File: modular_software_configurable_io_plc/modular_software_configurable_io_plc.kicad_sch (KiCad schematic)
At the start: 8 parts, among them J1 FW-14-03-G-D-085-315, J2 FW-02-03-G-D-085-315, J3 FW-02-03-G-D-085-315, J4 FW-04-03-G-D-085-315, J5 FW-04-03-G-D-085-315, J6 FW-02-03-G-D-085-315, J7 FW-02-03-G-D-085-315, J8 FW-14-03-G-D-085-315

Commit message: Minor updates to project files
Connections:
- net GNDA: now also J1.1, J1.11, J1.13, J1.15, J1.17, J1.19, J1.21, J1.23, J1.25, J1.27, J1.3, J1.5, J1.7, J1.9, J8.10, J8.12, J8.14, J8.16, J8.18, J8.2, J8.20, J8.22, J8.24, J8.26, J8.28, J8.4, J8.6, J8.8

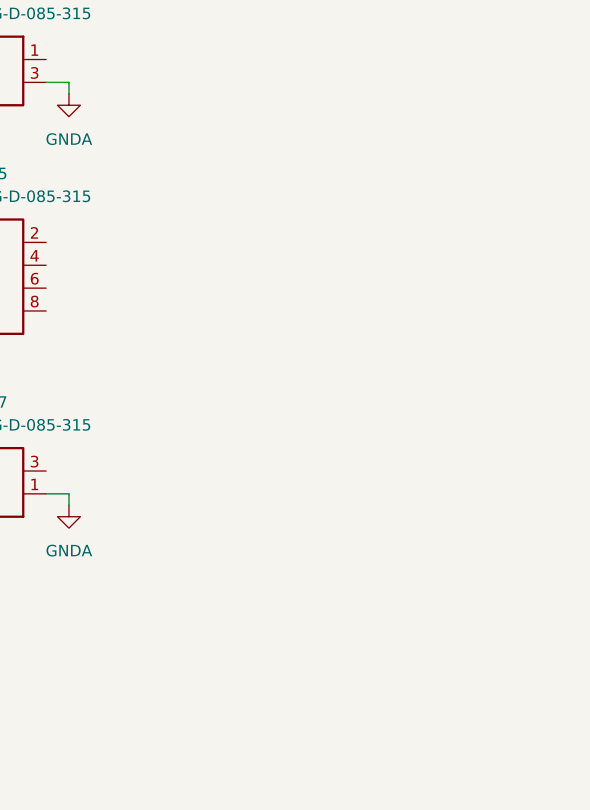
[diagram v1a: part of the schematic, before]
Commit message: Update KiCAD Symbol Generator submodule and add ibom configuration file
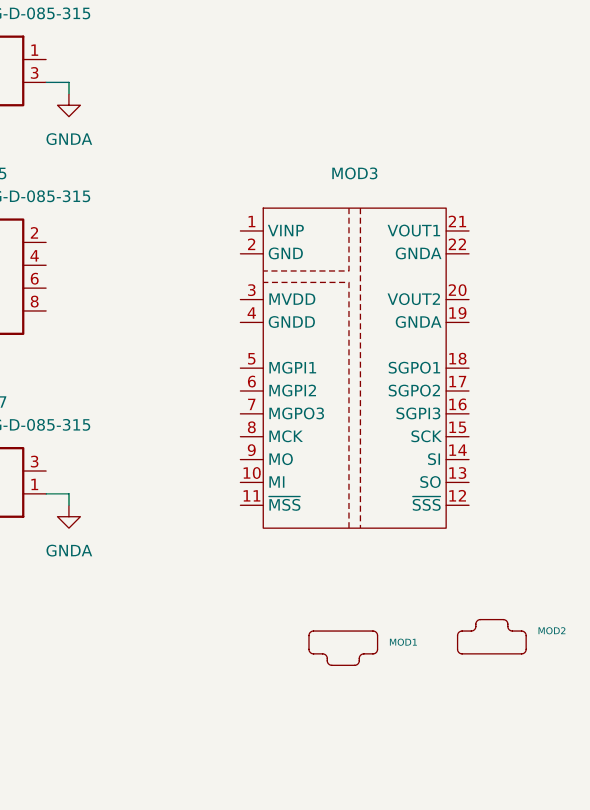
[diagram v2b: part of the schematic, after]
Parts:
- added MOD1: ~, modules_footprints:minimal_ad74413r, symbol UNITED_MODULES_DATA_BASE:MINIMAL_AD74413R
- added MOD2: ~, modules_footprints:minimal_max14906, symbol UNITED_MODULES_DATA_BASE:MINIMAL_MAX14906
- added MOD3: ~, modules_footprints:minimal_adp1032, symbol UNITED_MODULES_DATA_BASE:MINIMAL_ADP1032
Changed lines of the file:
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@@
+	)
+	(symbol
+		(lib_id "UNITED_MODULES_DATA_BASE:MINIMAL_ADP1032")
+		(at 217.17 100.33 0)
+		(unit 1)
+		(exclude_from_sim no)
+		(in_bom yes)
+		(on_board yes)
+		(dnp no)
+		(fields_autoplaced yes)
+		(property "Reference" "MOD3"
+			(at 217.17 78.74 0)
+			(effects
+				(font
+					(size 1.27 1.27)
+				)
+			)
+		)
+		(property "Value" "~"
+			(at 217.17 81.28 0)
+			(effects
+				(font
+					(size 1.27 1.27)
+				)
+			)
+		)
+		(property "Footprint" "modules_footprints:minimal_adp1032"
+			(at 227.33 120.65 0)
+			(effects
+				(font
+					(size 1.27 1.27)
+				)
+				(justify left)
+				(hide yes)
+			)
+		)
+		(property "Datasheet" ""
+			(at 217.17 95.25 0)
+			(effects
+				(font
+					(size 1.27 1.27)
+				)
+				(hide yes)
+			)
+		)
+		(property "Description" ""
+			(at 217.17 95.25 0)
+			(effects
+				(font
+					(size 1.27 1.27)
+				)
+				(hide yes)
+			)
+		)
+		(pin "13"
+		)
+		(pin "10"
+		)
+		(pin "19"
+		)
+		(pin "2"
+		)
+		(pin "17"
+		)
+		(pin "20"
+		)
+		(pin "15"
+		)
+		(pin "22"
+		)
+		(pin "7"
+		)
+		(pin "16"
+		)
+		(pin "8"
+		)
+		(pin "12"
+		)
+		(pin "4"
+		)
+		(pin "5"
+		)
+		(pin "3"
+		)
+		(pin "18"
+		)
+		(pin "6"
+		)
+		(pin "11"
+		)
+		(pin "14"
+		)
+		(pin "21"
+		)
+		(pin "1"
+		)
+		(pin "9"
+		)
+		(instances
+			(project ""
+				(path "/b764ffe3-5231-4422-b46d-b0de4c44c7b4"
+					(reference "MOD3")
+					(unit 1)
+				)
+			)
+		)
 	)
 	(symbol
@@
 	)
 	(symbol
+		(lib_id "UNITED_MODULES_DATA_BASE:MINIMAL_AD74413R")
+		(at 215.9 130.81 0)
+		(unit 1)
+		(exclude_from_sim no)
+		(in_bom yes)
+		(on_board yes)
+		(dnp no)
+		(fields_autoplaced yes)
+		(property "Reference" "MOD1"
+			(at 220.98 130.81 0)
+			(effects
+				(font
+					(size 0.762 0.762)
+				)
+				(justify left)
+			)
+		)
+		(property "Value" "~"
+			(at 220.98 132.08 0)
+			(effects
+				(font
+					(size 1.27 1.27)
+				)
+				(justify left)
+			)
+		)
+		(property "Footprint" "modules_footprints:minimal_ad74413r"
+			(at 218.44 135.89 0)
+			(effects
+				(font
+					(size 1.27 1.27)
+				)
+				(justify left)
+				(hide yes)
+			)
+		)
+		(property "Datasheet" ""
+			(at 215.9 130.81 0)
+			(effects
+				(font
+					(size 1.27 1.27)
+				)
+				(hide yes)
+			)
+		)
+		(property "Description" ""
+			(at 215.9 130.81 0)
+			(effects
+				(font
+					(size 1.27 1.27)
+				)
+				(hide yes)
+			)
+		)
+		(instances
+			(project ""
+				(path "/b764ffe3-5231-4422-b46d-b0de4c44c7b4"
+					(reference "MOD1")
+					(unit 1)
+				)
+			)
+		)
+	)
+	(symbol
 		(lib_id "power:GNDA")
 		(at 185.42 69.85 0)
@@
 					(unit 1)
 				)
+			)
+		)
+	)
+	(symbol
+		(lib_id "UNITED_MODULES_DATA_BASE:MINIMAL_MAX14906")
+		(at 232.41 130.81 0)
+		(unit 1)
+		(exclude_from_sim no)
+		(in_bom yes)
+		(on_board yes)
+		(dnp no)
+		(fields_autoplaced yes)
+		(property "Reference" "MOD2"
+			(at 237.49 129.54 0)
+			(effects
+				(font
+					(size 0.762 0.762)
+				)
+				(justify left)
+			)
+		)
+		(property "Value" "~"
+			(at 237.49 130.81 0)
+			(effects
+				(font
+					(size 1.27 1.27)
+				)
+				(justify left)
+			)
+		)
+		(property "Footprint" "modules_footprints:minimal_max14906"
+			(at 234.95 133.35 0)
+			(effects
+				(font
+					(size 1.27 1.27)
+				)
+				(justify left)
+				(hide yes)
+			)
+		)
+		(property "Datasheet" ""
+			(at 232.41 130.81 0)
+			(effects
+				(font
+					(size 1.27 1.27)
+				)
+				(hide yes)
+			)
+		)
+		(property "Description" ""
+			(at 232.41 130.81 0)
+			(effects
+				(font
+					(size 1.27 1.27)
+				)
+				(hide yes)
+			)
+		)
+		(instances
+			(project ""
+				(path "/b764ffe3-5231-4422-b46d-b0de4c44c7b4"
+					(reference "MOD2")
+					(unit 1)
+				)

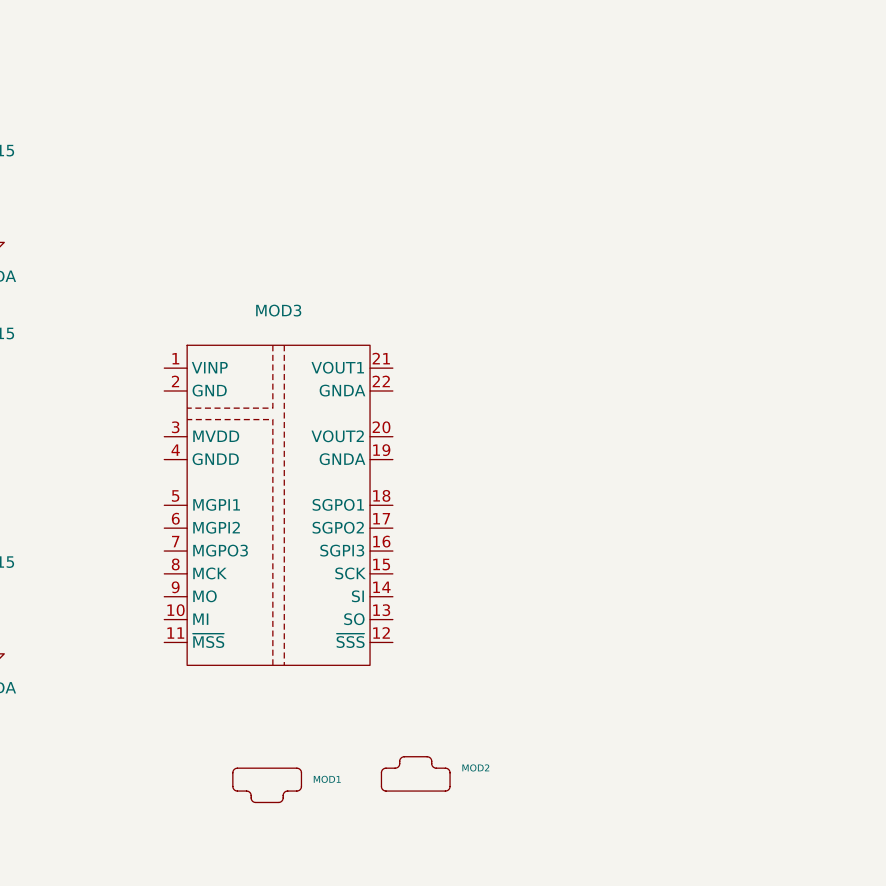
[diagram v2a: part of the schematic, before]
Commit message: Update KiCAD Symbol Generator submodule to latest commit
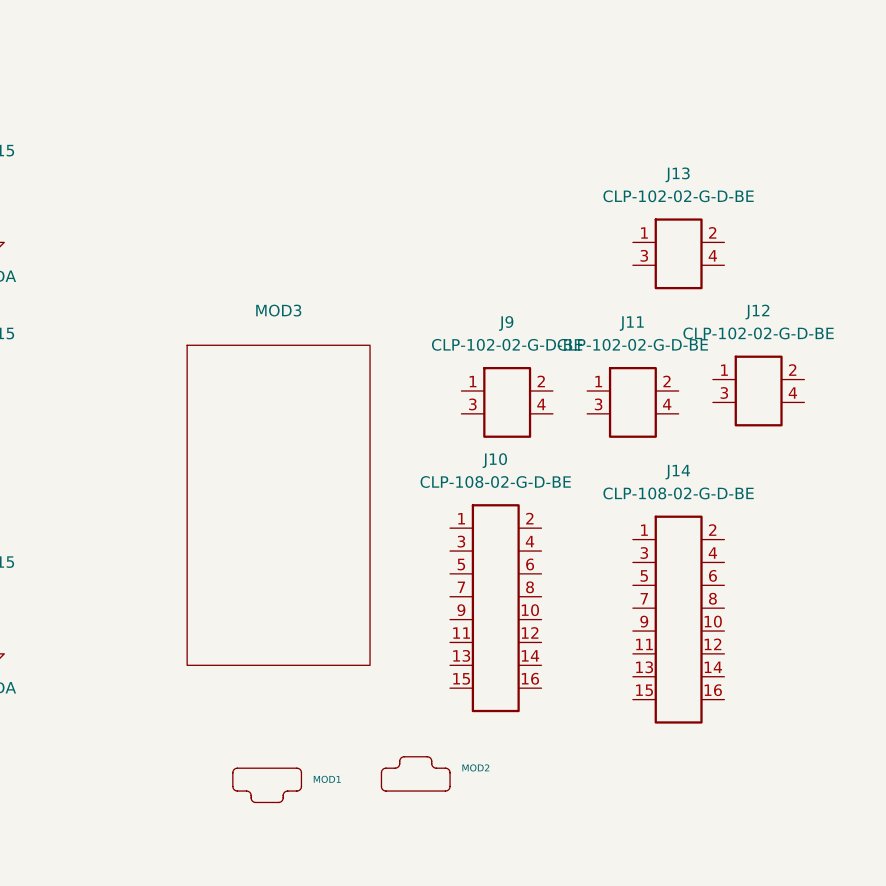
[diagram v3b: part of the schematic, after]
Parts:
- added J10, J14: CLP-108-02-G-D-BE, connector_footprints:CLP-108-02-G-D-BE, symbol UNITED_CONNECTORS_DATA_BASE:J_CLP-108-02-G-D-BE
- added J11, J12, J13, J9: CLP-102-02-G-D-BE, connector_footprints:CLP-102-02-G-D-BE, symbol UNITED_CONNECTORS_DATA_BASE:J_CLP-102-02-G-D-BE

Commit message: Minor updates
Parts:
- J1: value FW-14-03-G-D-085-315 -> FW-14-03-G-D-085-155; footprint connector_footprints:FW-14-03-G-D-085-315 -> connector_footprints:FW-14-03-G-D-085-155; symbol UNITED_CONNECTORS_DATA_BASE:J_FW-14-03-G-D-085-315 -> UNITED_CONNECTORS_DATA_BASE:J_FW-14-03-G-D-085-155; MPN FW-14-03-G-D-085-315 -> FW-14-03-G-D-085-155; Series FW-xx-03-G-D-085-315 -> FW-xx-03-G-D-085-155; Symbol Name J_FW-14-03-G-D-085-315 -> J_FW-14-03-G-D-085-155; Trustedparts Search https://www.trustedparts.com/en/search/FW-14-03-G-D-085-315 -> https://www.trustedparts.com/en/search/FW-14-03-G-D-085-155
- J2, J3, J6, J7: value FW-02-03-G-D-085-315 -> CLP-102-02-G-D-BE; footprint connector_footprints:FW-02-03-G-D-085-315 -> connector_footprints:CLP-102-02-G-D-BE; symbol UNITED_CONNECTORS_DATA_BASE:J_FW-02-03-G-D-085-315 -> UNITED_CONNECTORS_DATA_BASE:J_CLP-102-02-G-D-BE; Contact Plating Gold -> Tin; MPN FW-02-03-G-D-085-315 -> CLP-102-02-G-D-BE; Mounting Style Surface Mount -> Through Hole; Series FW-xx-03-G-D-085-315 -> CLP-1xx-02-G-D-BE; Symbol Name J_FW-02-03-G-D-085-315 -> J_CLP-102-02-G-D-BE; Trustedparts Search https://www.trustedparts.com/en/search/FW-02-03-G-D-085-315 -> https://www.trustedparts.com/en/search/CLP-102-02-G-D-BE
- J4, J5: value FW-04-03-G-D-085-315 -> CLP-104-02-G-D-BE; footprint connector_footprints:FW-04-03-G-D-085-315 -> connector_footprints:CLP-104-02-G-D-BE; symbol UNITED_CONNECTORS_DATA_BASE:J_FW-04-03-G-D-085-315 -> UNITED_CONNECTORS_DATA_BASE:J_CLP-104-02-G-D-BE; Contact Plating Gold -> Tin; MPN FW-04-03-G-D-085-315 -> CLP-104-02-G-D-BE; Mounting Style Surface Mount -> Through Hole; Series FW-xx-03-G-D-085-315 -> CLP-1xx-02-G-D-BE; Symbol Name J_FW-04-03-G-D-085-315 -> J_CLP-104-02-G-D-BE; Trustedparts Search https://www.trustedparts.com/en/search/FW-04-03-G-D-085-315 -> https://www.trustedparts.com/en/search/CLP-104-02-G-D-BE
- J8: value FW-14-03-G-D-085-315 -> CLP-114-02-G-D-BE; footprint connector_footprints:FW-14-03-G-D-085-315 -> connector_footprints:CLP-114-02-G-D-BE; symbol UNITED_CONNECTORS_DATA_BASE:J_FW-14-03-G-D-085-315 -> UNITED_CONNECTORS_DATA_BASE:J_CLP-114-02-G-D-BE; Contact Plating Gold -> Tin; MPN FW-14-03-G-D-085-315 -> CLP-114-02-G-D-BE; Mounting Style Surface Mount -> Through Hole; Series FW-xx-03-G-D-085-315 -> CLP-1xx-02-G-D-BE; Symbol Name J_FW-14-03-G-D-085-315 -> J_CLP-114-02-G-D-BE; Trustedparts Search https://www.trustedparts.com/en/search/FW-14-03-G-D-085-315 -> https://www.trustedparts.com/en/search/CLP-114-02-G-D-BE

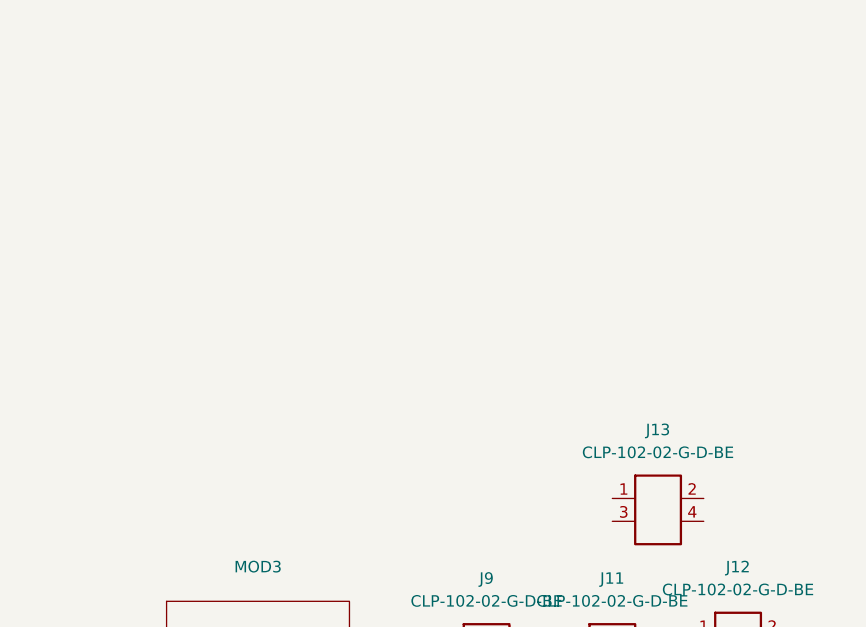
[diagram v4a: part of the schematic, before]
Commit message: Update KiCAD Symbol Generator submodule to latest commit
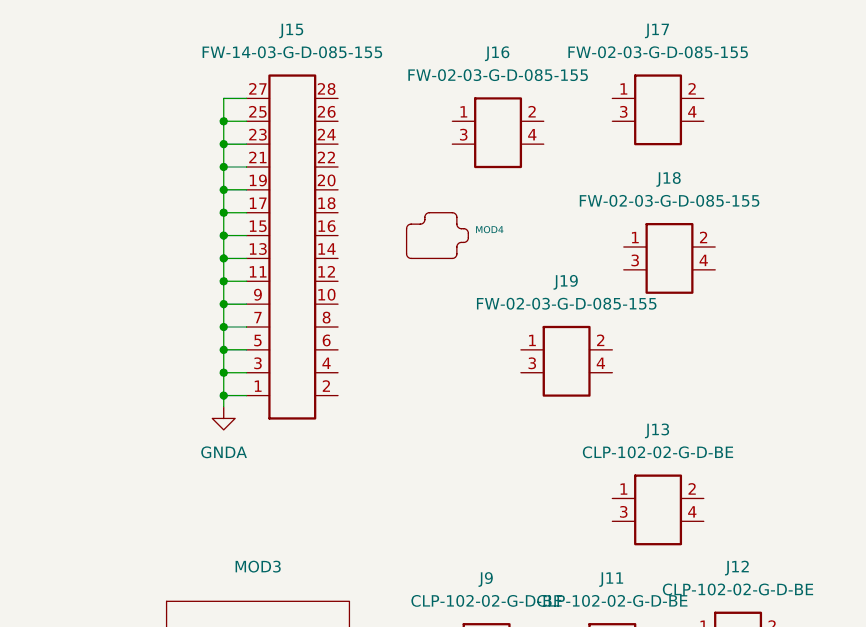
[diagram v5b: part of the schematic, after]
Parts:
- added J15: FW-14-03-G-D-085-155, connector_footprints:FW-14-03-G-D-085-155, symbol UNITED_CONNECTORS_DATA_BASE:J_FW-14-03-G-D-085-155
- added J16, J17, J18, J19: FW-02-03-G-D-085-155, connector_footprints:FW-02-03-G-D-085-155, symbol UNITED_CONNECTORS_DATA_BASE:J_FW-02-03-G-D-085-155
- added MOD4: ~, modules_footprints:minimal_adin1110, symbol UNITED_MODULES_DATA_BASE:MINIMAL_ADIN1110
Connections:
- net GNDA: now also J15.1, J15.11, J15.13, J15.15, J15.17, J15.19, J15.21, J15.23, J15.25, J15.27, J15.3, J15.5, J15.7, J15.9

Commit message: Backup
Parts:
- added J20, J21: CLP-102-02-G-D-BE, connector_footprints:CLP-102-02-G-D-BE, symbol UNITED_CONNECTORS_DATA_BASE:J_CLP-102-02-G-D-BE
- added MOD5: ~, modules_footprints:minimal_ltc9111, symbol UNITED_MODULES_DATA_BASE:MINIMAL_LTC9111

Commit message: Backup
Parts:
- MOD3, MOD5: 3dviewer Link (none) -> https://3dviewer.net/index.html#model=https://github.com/io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
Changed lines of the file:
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@@
+			)
+		)
+		(property "3dviewer Link" "https://3dviewer.net/index.html#model=https://github.com/ionutms/KiCAD_Symbols_Generator/blob/main/3D_models/minimal_adp1032.wrl"
+			(at 227.33 123.19 0)
+			(effects
+				(font
+					(size 1.27 1.27)
+				)
+				(justify left)
+				(hide yes)
 			)
 		)
@@
 				(hide yes)
 			)
+		)
+		(property "3dviewer Link" "https://3dviewer.net/index.html#model=https://github.com/ionutms/KiCAD_Symbols_Generator/blob/main/3D_models/minimal_ltc9111.wrl"
+			(at 323.85 83.82 0)
+			(effects
+				(font
+					(size 1.27 1.27)
+				)
+				(justify left)
+				(hide yes)
+			)

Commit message: Backup
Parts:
- added J22: TBP02R2-381-03BE, connector_footprints:TBP02R2-381-03BE, symbol UNITED_CONNECTORS_DATA_BASE:J_TBP02R2-381-03BE
- added J23: TBP02R2-381-08BE, connector_footprints:TBP02R2-381-08BE, symbol UNITED_CONNECTORS_DATA_BASE:J_TBP02R2-381-08BE
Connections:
- net GNDA: now also J12.1, J12.3, J13.2, J13.4, J14.1, J14.11, J14.13, J14.15, J14.2, J14.3, J14.5, J14.7, J14.9
- net GND: now reaches J10.1
- net GND: now also J10.11, J10.13, J10.15, J10.2, J10.3, J10.5, J10.7, J10.9, J11.1, J11.3, J9.1, J9.3
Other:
- moved on the sheet: J10, J11, J12, J13, J14, J9
